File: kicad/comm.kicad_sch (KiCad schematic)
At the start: 36 parts, among them J401 HR911105A, J402 RS485, U400 W5500, U401 SP3485EN, Y401 25MHz 18pF

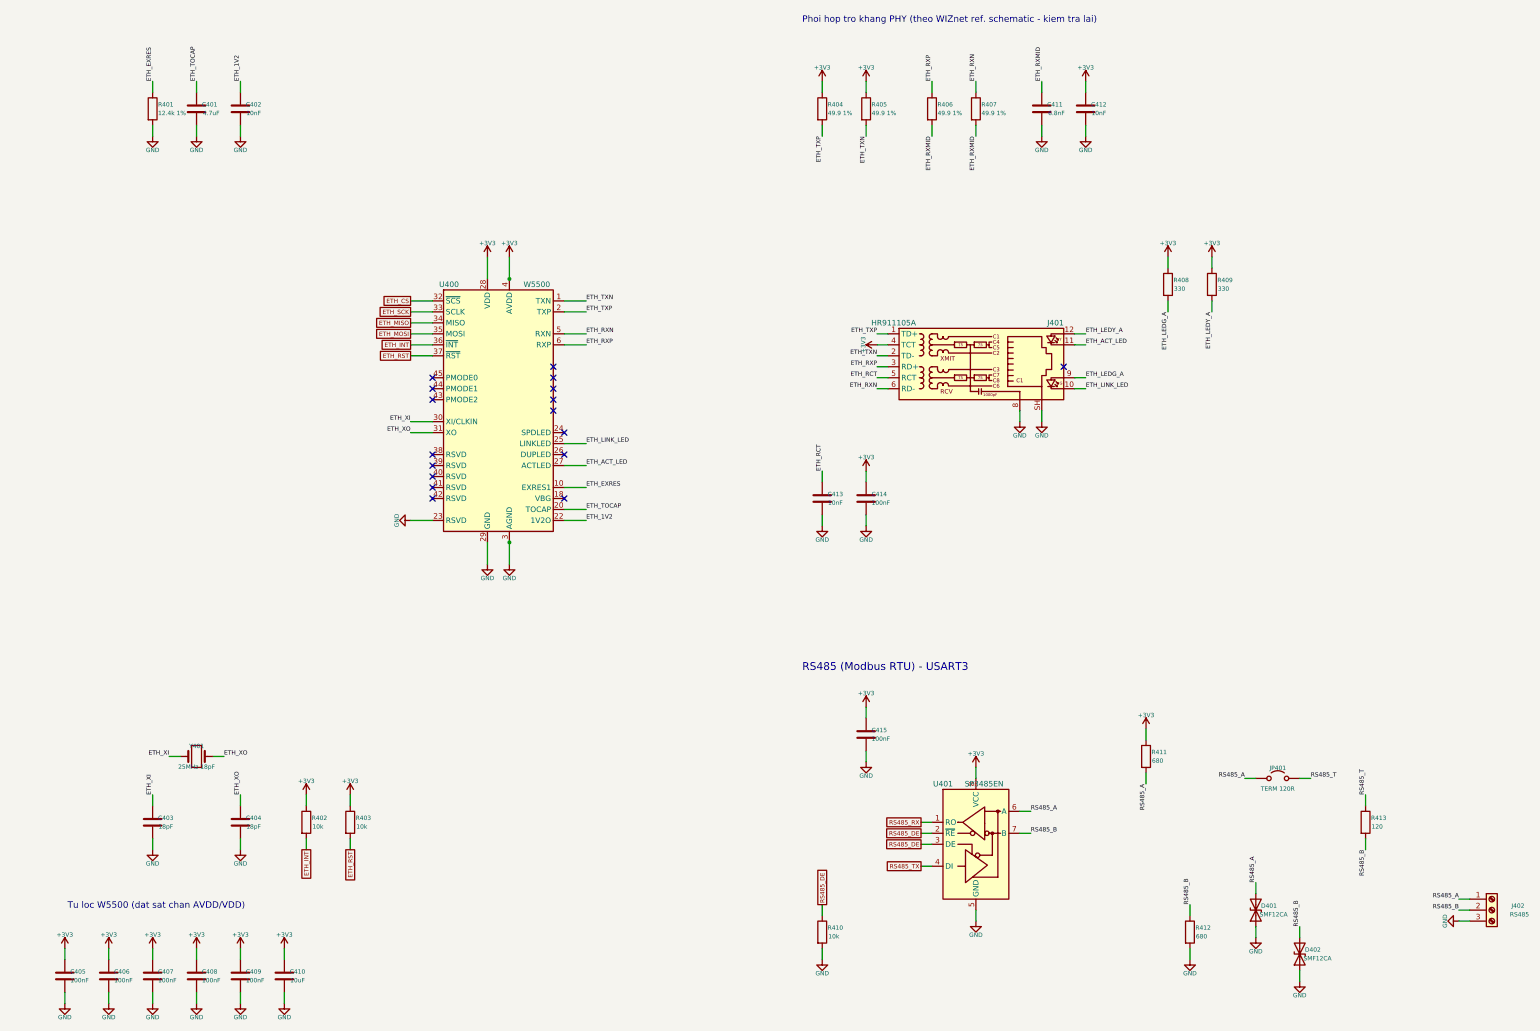
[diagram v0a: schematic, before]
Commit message: - bỏ các mạch 0-10v, RS485 RTU
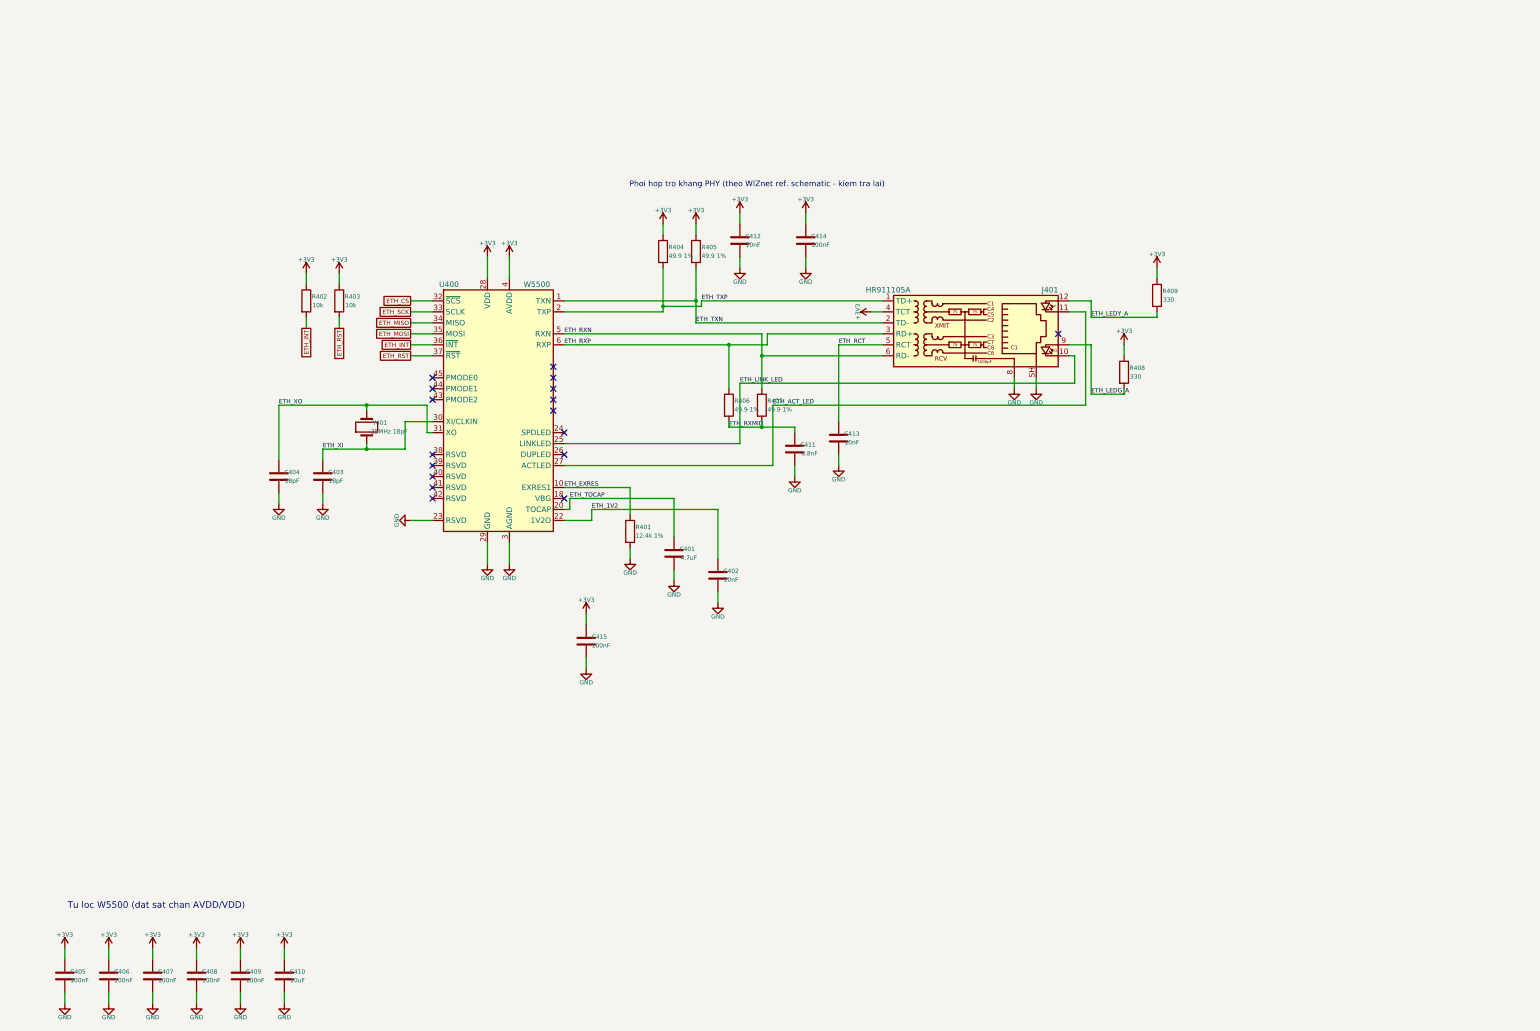
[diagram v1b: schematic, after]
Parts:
- removed D401, D402: SMF12CA, Diode_SMD:D_SOD-123F, symbol Device:D_TVS
- removed J402: RS485, TerminalBlock_Phoenix:TerminalBlock_Phoenix_MKDS-1-3-3.81_1x03_P3.81mm_Horizontal, symbol Connector:Screw_Terminal_01x03
- removed JP401: TERM 120R, Connector_PinHeader_2.54mm:PinHeader_1x02_P2.54mm_Vertical, symbol Jumper:Jumper_2_Open
- removed R410: 10k, Resistor_SMD:R_0603_1608Metric, symbol Device:R
- removed R411, R412: 680, Resistor_SMD:R_0603_1608Metric, symbol Device:R
- removed R413: 120, Resistor_SMD:R_1206_3216Metric, symbol Device:R
- removed U401: SP3485EN, Package_SO:SOIC-8_3.9x4.9mm_P1.27mm, symbol Interface_UART:SP3485EN
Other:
- note removed: "RS485 (Modbus RTU) - USART3"
- title: W5500 Ethernet (Modbus TCP) + RS485 (Modbus RTU) -> W5500 Ethernet - Modbus TCP

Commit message: - bỏ các cầu chì thêm mô tả cho từng linh kiên
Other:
- note added: "8 socket = tối đa 8 kết nối Modbus TCP đồng thời. Giao tiếp MCU qua SPI2 (≤ 21MHz)."
- note added: "C401 4.7µF (TOCAP), C402 10nF (1V2O): bắt buộc theo datasheet."
- note added: "C405–C409 100nF: một tụ cho mỗi chân AVDD; C410 10µF dự trữ (W5500 hút ~130mA dạng xung khi phát)."
- note added: "C415 100nF: lọc chân VDD (pin 28) W5500."
- note added: "LED RJ45 (W5500 kéo xuống để sáng): I = (3.3 − 2.0)/330Ω ≈ 4mA."
- note added: "R401 12.4kΩ 1% (EXRES1): tham chiếu dòng bias PHY – giá trị theo datasheet."
- note added: "R402, R403 10k kéo lên INT, RST (giữ mức 1 khi MCU chưa khởi động)."
- note added: "RJ45 HR911105A có biến áp cách ly 1500Vrms. TCT → 3.3V (C414 lọc); RCT → C413 10nF xuống GND."
- note added: "RX: R406, R407 49.9Ω phối hợp 100Ω; C411 6.8nF nối điểm giữa xuống GND (xoay chiều)."
- note added: "TX: R404, R405 49.9Ω kéo lên 3.3V (tầng phát nguồn dòng). Cáp Cat5 Z_vi sai = 100Ω = 2 × 49.9Ω. C412 10nF lọc nguồn."
- note added: "W5500 – ETHERNET 10/100 + TCP/IP PHẦN CỨNG"
- note added: "Y401 25MHz ±50ppm (chuẩn Ethernet). Tụ tải C = 2·(C_L − C_stray) = 2 × (11 − 2) ≈ 18pF."

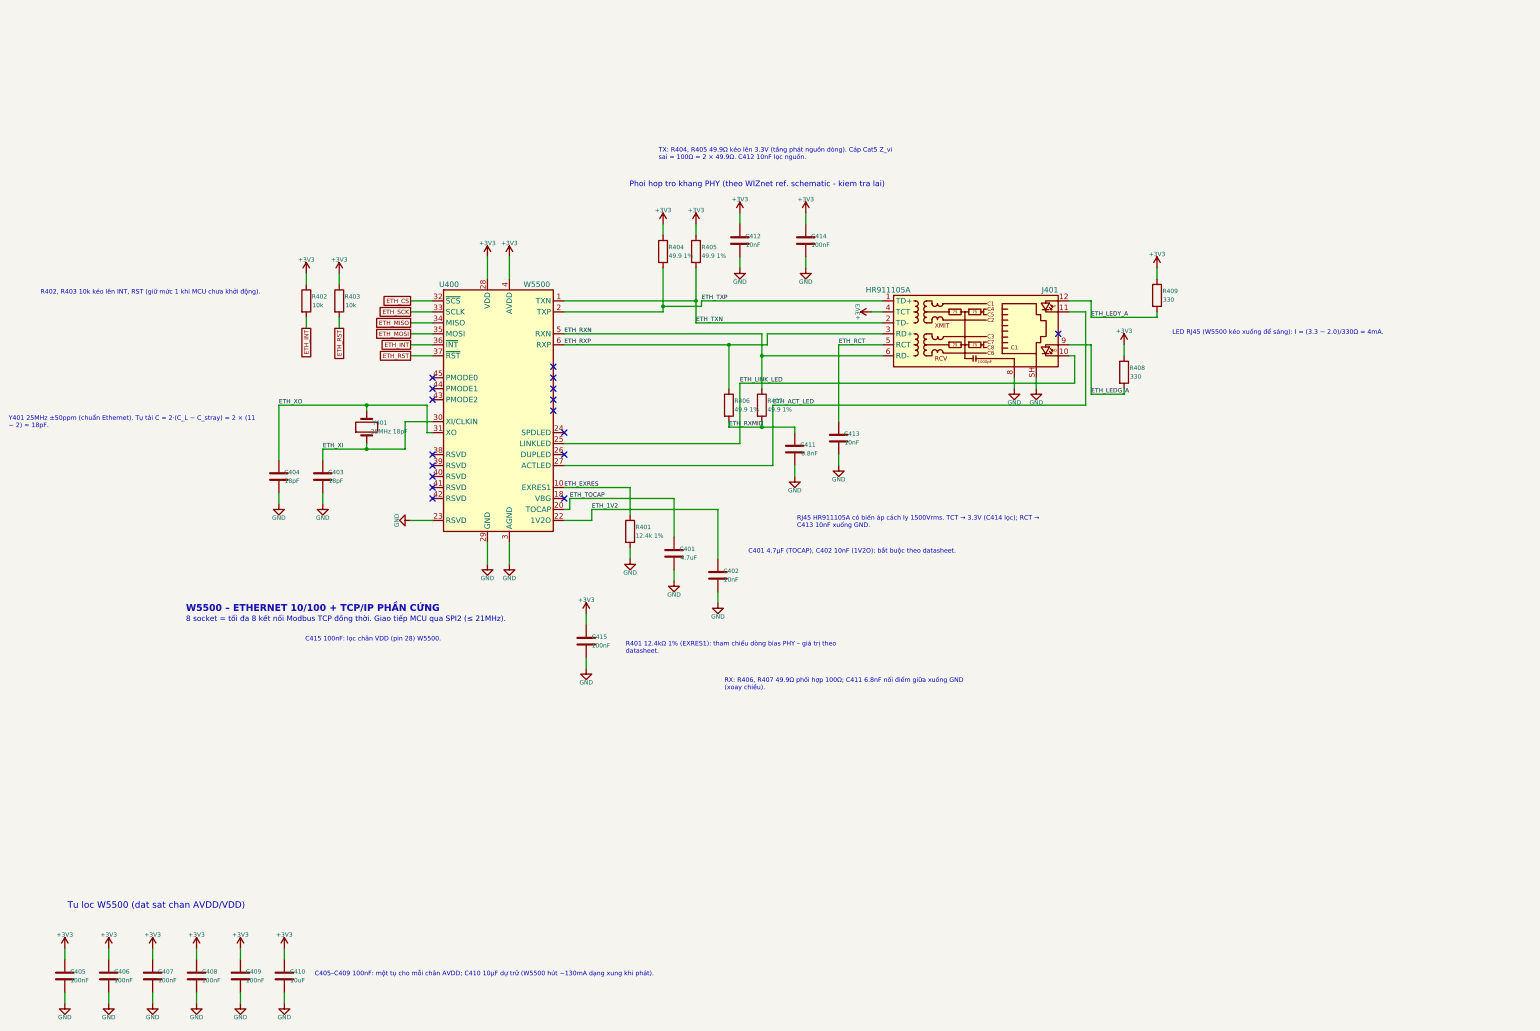
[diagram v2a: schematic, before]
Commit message: - thay w5500 bằng module w5500 lite
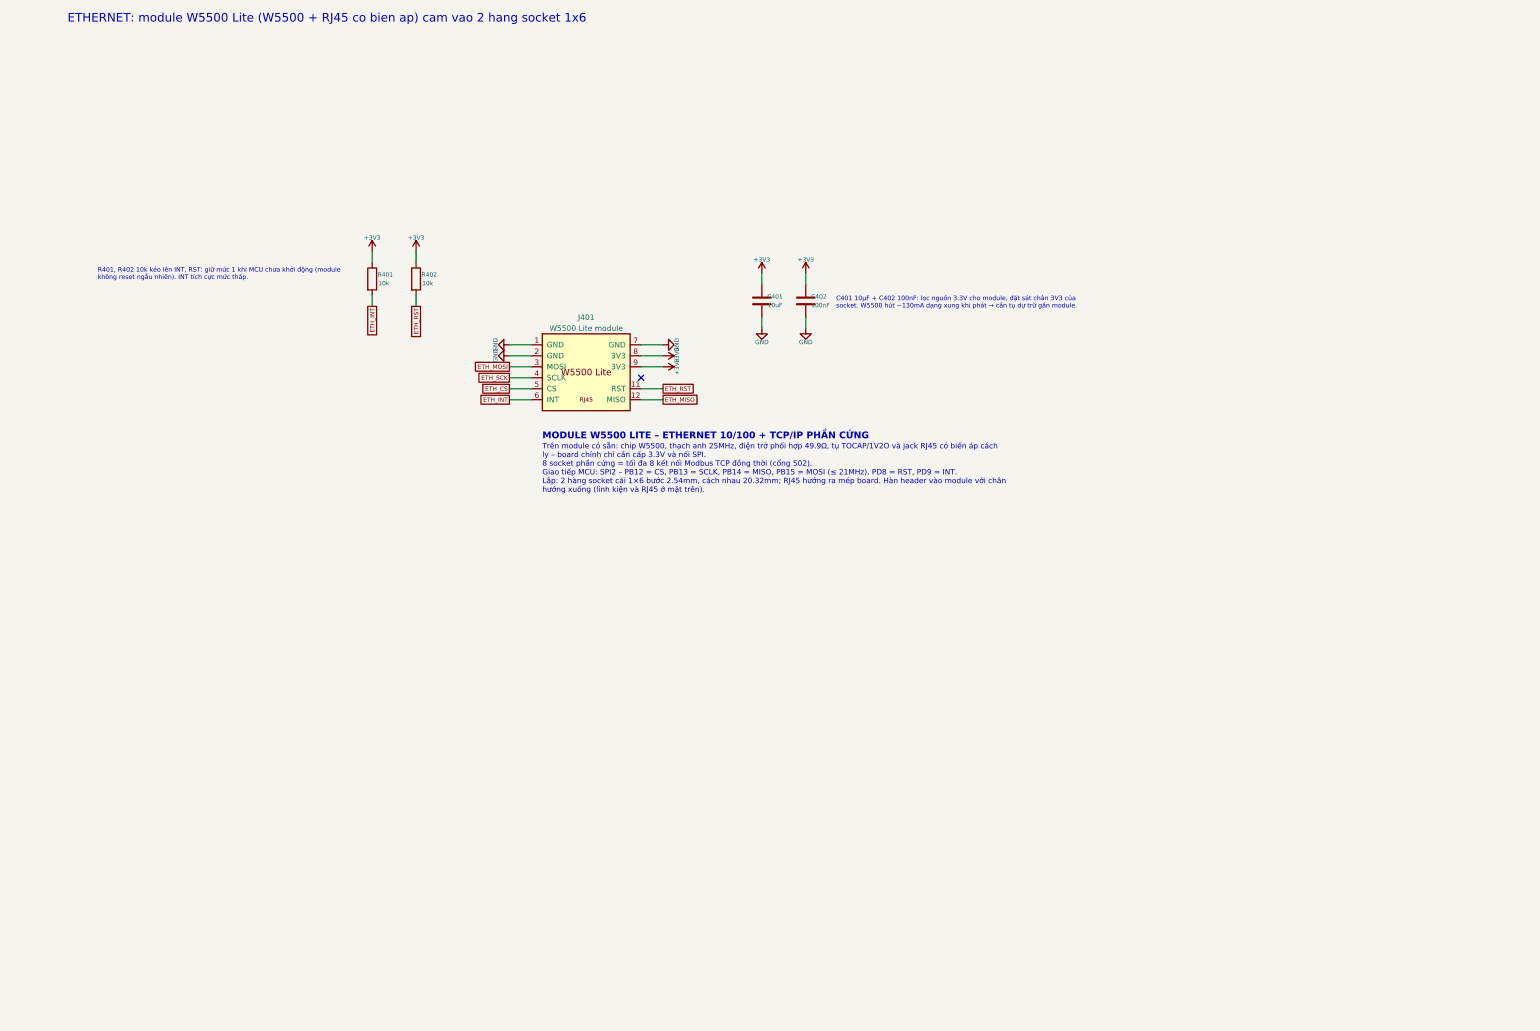
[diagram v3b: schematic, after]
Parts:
- removed C403, C404: 18pF, Capacitor_SMD:C_0603_1608Metric, symbol Device:C
- removed C405, C406, C407, C408, C409, C414, C415: 100nF, Capacitor_SMD:C_0603_1608Metric, symbol Device:C
- removed C410: 10uF, Capacitor_SMD:C_0805_2012Metric, symbol Device:C
- removed C411: 6.8nF, Capacitor_SMD:C_0603_1608Metric, symbol Device:C
- removed C412, C413: 10nF, Capacitor_SMD:C_0603_1608Metric, symbol Device:C
- removed J401: HR911105A, Connector_RJ:RJ45_Hanrun_HR911105A_Horizontal, symbol Connector:RJ45_Hanrun_HR911105A_Horizontal
- removed R403: 10k, Resistor_SMD:R_0603_1608Metric, symbol Device:R
- removed R404, R405, R406, R407: 49.9 1%, Resistor_SMD:R_0603_1608Metric, symbol Device:R
- removed R408, R409: 330, Resistor_SMD:R_0603_1608Metric, symbol Device:R
- removed U400: W5500, Package_QFP:LQFP-48_7x7mm_P0.5mm, symbol Interface_Ethernet:W5500
- removed Y401: 25MHz 18pF, Crystal:Crystal_SMD_3225-4Pin_3.2x2.5mm, symbol Device:Crystal
- added J401: W5500 Lite module, PLC:W5500_Lite_Module, symbol PLC:W5500_Lite
- C401: value 4.7uF -> 10uF
- C402: value 10nF -> 100nF
- R401: value 12.4k 1% -> 10k
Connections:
- net ETH_1V2 is gone; now on net +3V3: C402.1
- net ETH_EXRES is gone; now on net +3V3: R401.1
- net ETH_TOCAP is gone; now on net +3V3: C401.1
- net +3V3: now also J401.8 (3V3), J401.9 (3V3)
- net ETH_CS: now also J401.5 (CS)
- net ETH_INT: now also R401.2, J401.6 (INT); no longer R402.2
- net ETH_MISO: now also J401.12 (MISO)
- net ETH_MOSI: now also J401.3 (MOSI)
- net ETH_RST: now also R402.2, J401.11 (RST)
- net ETH_SCK: now also J401.4 (SCLK)
- net GND: now also J401.1 (GND), J401.2 (GND), J401.7 (GND); no longer R401.2
- no-connect marks 17 -> 1
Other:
- note added: "C401 10µF + C402 100nF: lọc nguồn 3.3V cho module, đặt sát chân 3V3 của socket. W5500 hút ~130mA dạng xung khi phát → cần tụ dự trữ gần module."
- note added: "ETHERNET: module W5500 Lite (W5500 + RJ45 co bien ap) cam vao 2 hang socket 1x6"
- note added: "MODULE W5500 LITE – ETHERNET 10/100 + TCP/IP PHẦN CỨNG"
- note added: "R401, R402 10k kéo lên INT, RST: giữ mức 1 khi MCU chưa khởi động (module không reset ngẫu nhiên). INT tích cực mức thấp."
- note added: "Trên module có sẵn: chip W5500, thạch anh 25MHz, điện trở phối hợp 49.9Ω, tụ TOCAP/1V2O và jack RJ45 có biến áp cách ly – board chính chỉ cần cấp 3.3V và nối SPI. 8 socket phần cứng = tối đa 8 kết nối Modbus TCP đồng thời (cổng 502). Giao tiếp MCU: SPI2 – PB12 = CS, PB13 = SCLK, PB14 = MISO, PB15 = MOSI (≤ 21MHz), PD8 = RST, PD9 = INT. Lắp: 2 hàng socket cái 1×6 bước 2.54mm, cách nhau 20.32mm; RJ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"
- note removed: "8 socket = tối đa 8 kết nối Modbus TCP đồng thời. Giao tiếp MCU qua SPI2 (≤ 21MHz)."
- note removed: "C401 4.7µF (TOCAP), C402 10nF (1V2O): bắt buộc theo datasheet."
- note removed: "C405–C409 100nF: một tụ cho mỗi chân AVDD; C410 10µF dự trữ (W5500 hút ~130mA dạng xung khi phát)."
- note removed: "C415 100nF: lọc chân VDD (pin 28) W5500."
- note removed: "LED RJ45 (W5500 kéo xuống để sáng): I = (3.3 − 2.0)/330Ω ≈ 4mA."
- note removed: "Phoi hop tro khang PHY (theo WIZnet ref. schematic - kiem tra lai)"
- note removed: "R401 12.4kΩ 1% (EXRES1): tham chiếu dòng bias PHY – giá trị theo datasheet."
- note removed: "R402, R403 10k kéo lên INT, RST (giữ mức 1 khi MCU chưa khởi động)."
- note removed: "RJ45 HR911105A có biến áp cách ly 1500Vrms. TCT → 3.3V (C414 lọc); RCT → C413 10nF xuống GND."
- note removed: "RX: R406, R407 49.9Ω phối hợp 100Ω; C411 6.8nF nối điểm giữa xuống GND (xoay chiều)."
- note removed: "TX: R404, R405 49.9Ω kéo lên 3.3V (tầng phát nguồn dòng). Cáp Cat5 Z_vi sai = 100Ω = 2 × 49.9Ω. C412 10nF lọc nguồn."
- note removed: "Tu loc W5500 (dat sat chan AVDD/VDD)"
- note removed: "W5500 – ETHERNET 10/100 + TCP/IP PHẦN CỨNG"
- note removed: "Y401 25MHz ±50ppm (chuẩn Ethernet). Tụ tải C = 2·(C_L − C_stray) = 2 × (11 − 2) ≈ 18pF."
- title: W5500 Ethernet - Modbus TCP -> Ethernet - module W5500 Lite (Modbus TCP)
